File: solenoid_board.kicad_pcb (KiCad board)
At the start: 2 copper layers, 48 parts, among them J2 MCU_LEFT_LEGS, J3 MCU_RIGHT_LEGS

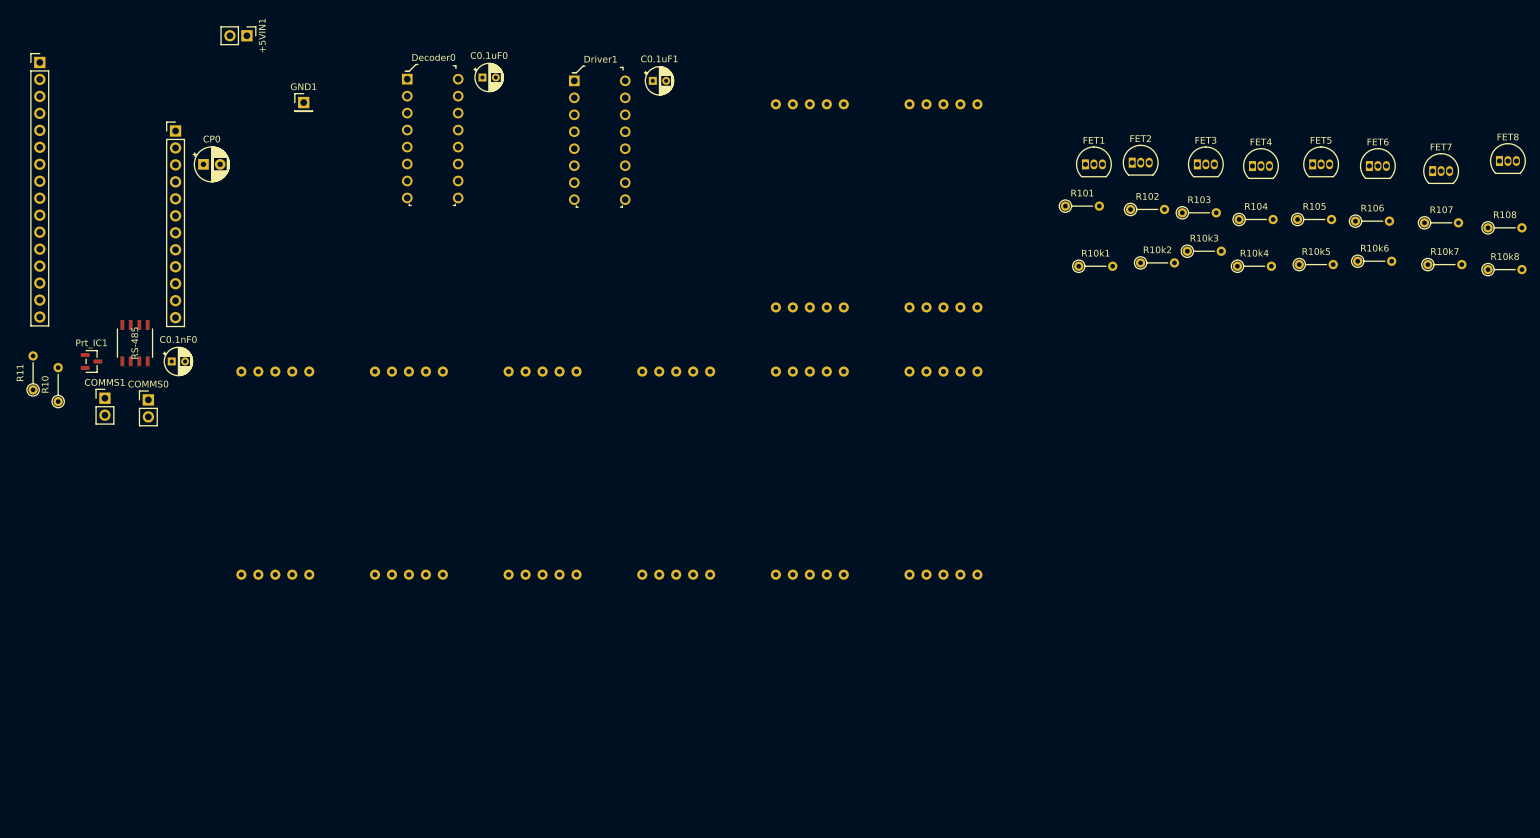
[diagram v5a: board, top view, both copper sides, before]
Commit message: Finished laying out Scoreboard PCB, good enough for government work.
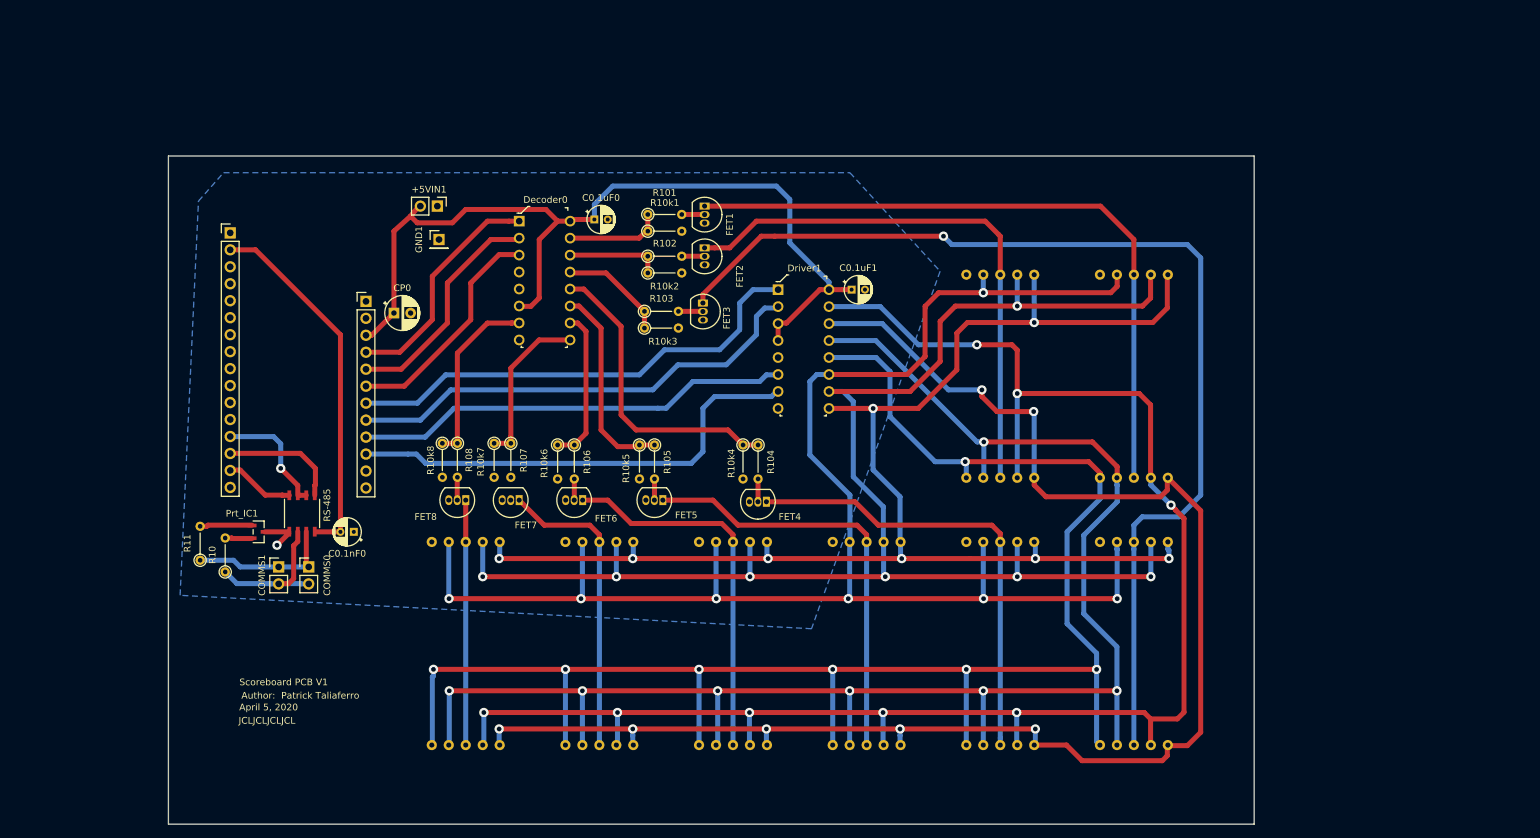
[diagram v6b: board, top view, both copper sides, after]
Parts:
- moved FET8 162.8 mm to (113.5, 94.0), turned to 180 degrees
- moved R10k8 158.6 mm to (110.0, 85.5), turned to 270 degrees
- moved R108 157.6 mm to (112.2, 85.5), turned to 270 degrees
- moved FET7 145.3 mm to (121.5, 94.0), turned to 180 degrees
- moved R10k7 142.3 mm to (117.8, 85.5), turned to 270 degrees
- moved R107 140.7 mm to (120.2, 85.5), turned to 270 degrees
- moved FET6 127.9 mm to (131.0, 94.0), turned to 180 degrees
- moved R10k6 122.9 mm to (127.2, 85.8), turned to 270 degrees
- moved R106 121.6 mm to (129.8, 85.8), turned to 270 degrees
- moved FET5 109.5 mm to (143.0, 94.0), turned to 180 degrees
- moved R10k5 102.4 mm to (139.5, 85.8), turned to 270 degrees
- moved R105 102.0 mm to (141.8, 85.8), turned to 270 degrees
- moved FET4 88.4 mm to (158.5, 94.2), turned to 180 degrees
- moved R10k3 82.1 mm to (140.2, 68.2)
- moved R103 81.8 mm to (140.2, 65.8)
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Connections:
- 7Seg_1 pad 5: /dp -> Net-(7Seg_1-Pad5)
- 7Seg_2 pad 5: /dp -> Net-(7Seg_2-Pad5)
- 7Seg_3 pad 5: /dp -> Net-(7Seg_3-Pad5)
- 7Seg_4 pad 5: /dp -> Net-(7Seg_4-Pad5)
- 7Seg_5 pad 5: /dp -> Net-(7Seg_5-Pad5)
- 7Seg_6 pad 5: /dp -> Net-(7Seg_6-Pad5)
- 7Seg_7 pad 5: /dp -> Net-(7Seg_7-Pad5)
- 7Seg_8 pad 5: /dp -> Net-(7Seg_8-Pad5)
- Driver1 pad 1: /D9 -> /D10
- Driver1 pad 2: /D6 -> /D9
- Driver1 pad 6: /D5 -> /D6
- Driver1 pad 7: /D10 -> /D5
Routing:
- net /b: track 0.00 -> 256.2 mm, vias 0 -> 7
- net /f: track 0.00 -> 253.7 mm, vias 0 -> 8
- net /a: track 0.00 -> 243.5 mm, vias 0 -> 7
- net /c: track 0.00 -> 238.4 mm, vias 0 -> 7
- net /g: track 0.00 -> 232.7 mm, vias 0 -> 7
- net /d: track 0.00 -> 224.1 mm, vias 0 -> 7
- net /e: track 0.00 -> 209.7 mm, vias 0 -> 8
- net /Third_Display: track 0.00 -> 161.1 mm, vias 0 -> 1
- net +5V: track 0.00 -> 134.2 mm
- net /First_Display: track 0.00 -> 102.1 mm
- net /Second_Display: track 0.00 -> 83.1 mm
- net /D10: track 0.00 -> 71.1 mm
- net /D9: track 0.00 -> 71.0 mm
- net /D5: track 0.00 -> 70.5 mm
- net /Fourth_Display: track 0.00 -> 68.9 mm
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- added copper zone on B.Cu, net GND
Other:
- board outline added: 162.5 x 100 mm
- board text added: "April 5, 2020"
- board text added: "Author: Patrick Taliaferro"
- board text added: "JCLJCLJCLJCL"
- board text added: "Scoreboard PCB V1"
